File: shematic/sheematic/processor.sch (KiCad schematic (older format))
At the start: 15 parts, among them J1 Conn_01x05_Male, J2 Conn_01x05_Male, J3 Conn_01x05_Male, J4 Conn_01x07_Male, J5 Conn_01x02_Male, J6 Conn_01x07_Male, J7 Conn_01x07_Male, J8 Conn_01x07_Male, U1 E73-2G4M04S-52832

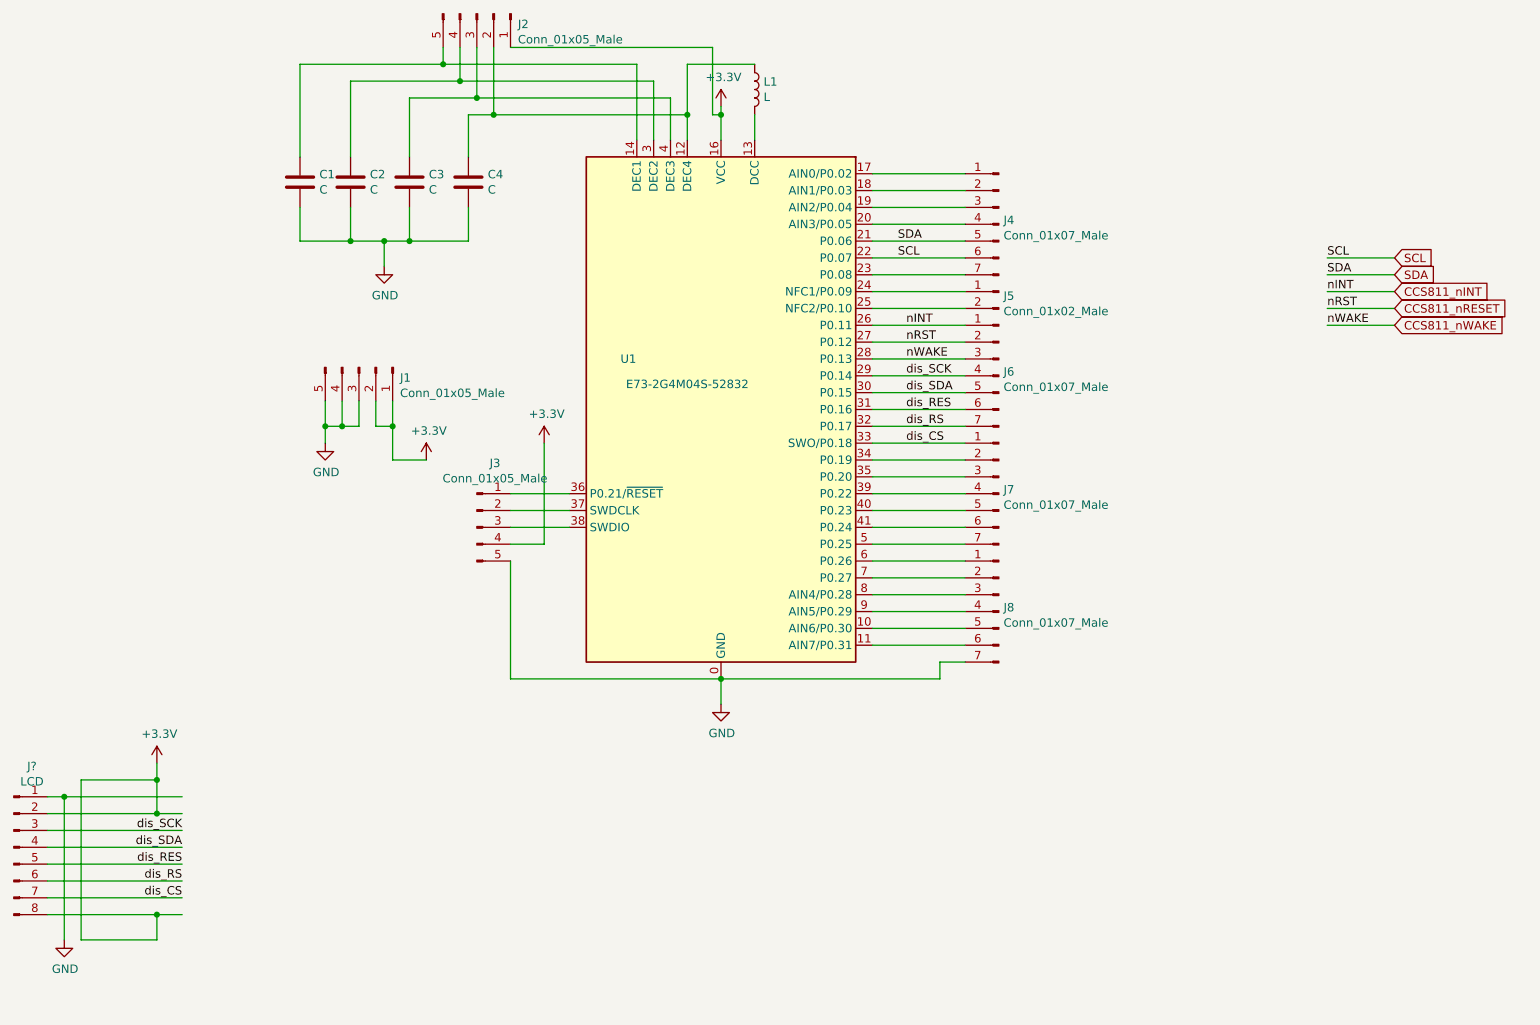
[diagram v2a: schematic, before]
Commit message: modify for warios drive
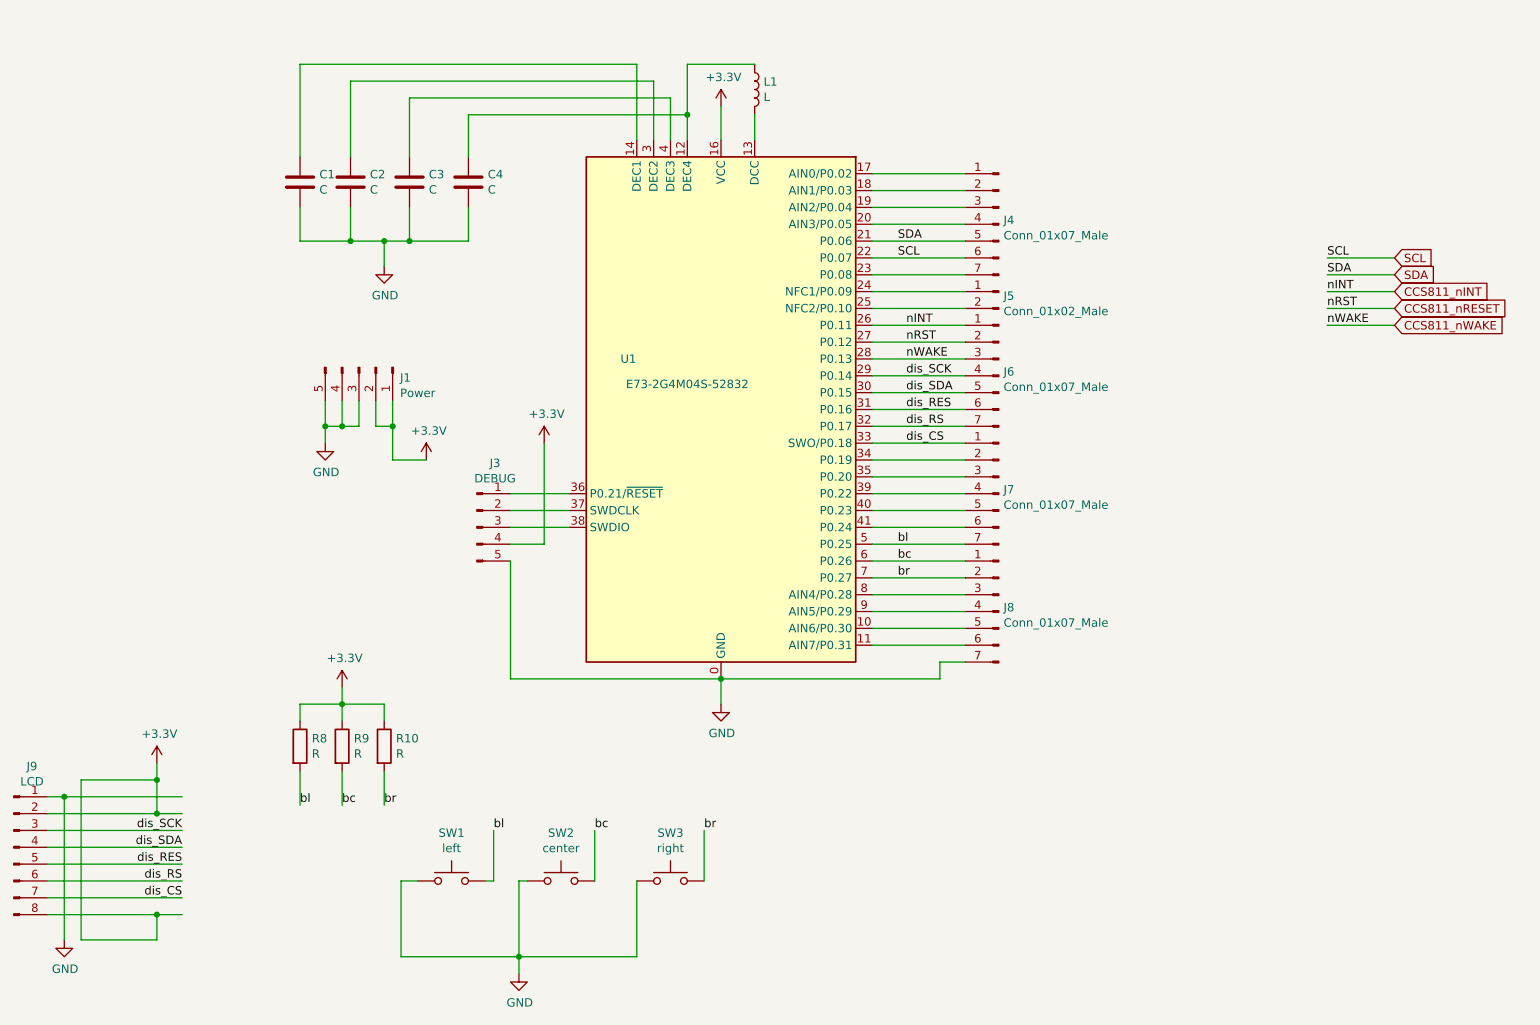
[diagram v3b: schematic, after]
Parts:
- removed J2: Conn_01x05_Male, symbol Connector:Conn_01x05_Male
- added R10, R8, R9: R, Resistor_SMD:R_0603_1608Metric_Pad1.05x0.95mm_HandSolder, symbol Device:R
- added SW1: left, Button_Switch_THT:SW_PUSH_6mm, symbol Switch:SW_Push
- added SW2: center, Button_Switch_THT:SW_PUSH_6mm, symbol Switch:SW_Push
- added SW3: right, Button_Switch_THT:SW_PUSH_6mm, symbol Switch:SW_Push
- C1, C2, C3, C4: footprint (none) -> Capacitor_SMD:C_0603_1608Metric_Pad1.08x0.95mm_HandSolder
- J1: value Conn_01x05_Male -> Power; footprint (none) -> Connector_PinHeader_2.54mm:PinHeader_1x05_P2.54mm_Vertical
- J3: value Conn_01x05_Male -> DEBUG; footprint (none) -> Connector_PinHeader_2.54mm:PinHeader_1x05_P2.54mm_Vertical
- J4, J6, J7, J8: footprint (none) -> Connector_PinHeader_2.54mm:PinHeader_1x07_P2.54mm_Vertical
- J5: footprint (none) -> Connector_PinHeader_2.54mm:PinHeader_1x02_P2.54mm_Vertical
- J9: renamed from J?; footprint (none) -> Connector_PinHeader_2.54mm:PinHeader_1x08_P2.54mm_Vertical
- L1: footprint (none) -> Inductor_SMD:L_0805_2012Metric_Pad1.15x1.40mm_HandSolder
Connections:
- net +3V3: now also R10.1, R8.1, R9.1
- net GND: now also SW1.1, SW2.1, SW3.1
- net bl: now reaches J7.7 (Pin_7), U1.5 (P0.25)
- net bl: now also R8.2, SW1.2
- net bc: now reaches J8.1 (Pin_1), U1.6 (P0.26)
- net bc: now also R9.2, SW2.2
- net br: now reaches J8.2 (Pin_2), U1.7 (P0.27)
- net br: now also R10.2, SW3.2
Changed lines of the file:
@@
 P 4700 3600
 F 0 "J3" H 4808 3981 50  0000 C CNN
-F 1 "Conn_01x05_Male" H 4808 3890 50  0000 C CNN
-F 2 "" H 4700 3600 50  0001 C CNN
+F 1 "DEBUG" H 4808 3890 50  0000 C CNN
+F 2 "Connector_PinHeader_2.54mm:PinHeader_1x05_P2.54mm_Vertical" H 4700 3600 50  0001 C CNN
 F 3 "~" H 4700 3600 50  0001 C CNN
 	1    4700 3600
@@
 	1    0    0    -1
 $EndComp
-Wire Wire Line
-	6150 1100 6150 1150
 $Comp
 L power:+3.3V #PWR04
@@
 F 0 "L1" H 6403 1046 50  0000 L CNN
 F 1 "L" H 6403 955 50  0000 L CNN
-F 2 "" H 6350 1000 50  0001 C CNN
+F 2 "Inductor_SMD:L_0805_2012Metric_Pad1.15x1.40mm_HandSolder" H 6350 1000 50  0001 C CNN
 F 3 "~" H 6350 1000 50  0001 C CNN
 	1    6350 1000
@@
 F 0 "C4" H 4765 1596 50  0000 L CNN
 F 1 "C" H 4765 1505 50  0000 L CNN
-F 2 "" H 4688 1400 50  0001 C CNN
+F 2 "Capacitor_SMD:C_0603_1608Metric_Pad1.08x0.95mm_HandSolder" H 4688 1400 50  0001 C CNN
 F 3 "~" H 4650 1550 50  0001 C CNN
 	1    4650 1550
@@
 F 0 "C3" H 4415 1596 50  0000 L CNN
 F 1 "C" H 4415 1505 50  0000 L CNN
-F 2 "" H 4338 1400 50  0001 C CNN
+F 2 "Capacitor_SMD:C_0603_1608Metric_Pad1.08x0.95mm_HandSolder" H 4338 1400 50  0001 C CNN
 F 3 "~" H 4300 1550 50  0001 C CNN
 	1    4300 1550
@@
 F 0 "C2" H 4065 1596 50  0000 L CNN
 F 1 "C" H 4065 1505 50  0000 L CNN
-F 2 "" H 3988 1400 50  0001 C CNN
+F 2 "Capacitor_SMD:C_0603_1608Metric_Pad1.08x0.95mm_HandSolder" H 3988 1400 50  0001 C CNN
 F 3 "~" H 3950 1550 50  0001 C CNN
 	1    3950 1550
@@
 F 0 "C1" H 3765 1596 50  0000 L CNN
 F 1 "C" H 3765 1505 50  0000 L CNN
-F 2 "" H 3688 1400 50  0001 C CNN
+F 2 "Capacitor_SMD:C_0603_1608Metric_Pad1.08x0.95mm_HandSolder" H 3688 1400 50  0001 C CNN
 F 3 "~" H 3650 1550 50  0001 C CNN
 	1    3650 1550
@@
 Wire Wire Line
 	4650 1400 4650 1150
-Wire Wire Line
-	4650 1150 4800 1150
 Connection ~ 5950 1150
 Wire Wire Line
@@
 	4300 1400 4300 1050
 Wire Wire Line
-	4300 1050 4700 1050
-Wire Wire Line
 	5850 1050 5850 1300
 Wire Wire Line
 	3950 1400 3950 950
 Wire Wire Line
-	3950 950  4600 950
-Wire Wire Line
 	5750 950  5750 1300
 Wire Wire Line
 	3650 1400 3650 850
-Wire Wire Line
-	3650 850  4500 850
 Wire Wire Line
 	5650 850  5650 1300
@@
 F 0 "J5" H 7772 2174 50  0000 R CNN
 F 1 "Conn_01x02_Male" H 7772 2083 50  0000 R CNN
-F 2 "" H 7800 2200 50  0001 C CNN
+F 2 "Connector_PinHeader_2.54mm:PinHeader_1x02_P2.54mm_Vertical" H 7800 2200 50  0001 C CNN
 F 3 "~" H 7800 2200 50  0001 C CNN
 	1    7800 2200
@@
 Wire Wire Line
 	7600 2300 7050 2300
-$Comp
-L Connector:Conn_01x05_Male J2
-U 1 1 602B2D83
-P 4700 550
-F 0 "J2" V 4762 794 50  0000 L CNN
-F 1 "Conn_01x05_Male" V 4853 794 50  0000 L CNN
-F 2 "" H 4700 550 50  0001 C CNN
-F 3 "~" H 4700 550 50  0001 C CNN
-	1    4700 550
-	0    1    1    0
-$EndComp
-Wire Wire Line
-	4500 750  4500 850
-Connection ~ 4500 850
-Wire Wire Line
-	4500 850  5650 850
-Wire Wire Line
-	4600 750  4600 950
-Connection ~ 4600 950
-Wire Wire Line
-	4600 950  5750 950
-Wire Wire Line
-	4700 750  4700 1050
-Connection ~ 4700 1050
-Wire Wire Line
-	4700 1050 5850 1050
-Wire Wire Line
-	4800 750  4800 1150
-Connection ~ 4800 1150
-Wire Wire Line
-	4800 1150 5950 1150
-Wire Wire Line
-	4900 750  6100 750
-Wire Wire Line
-	6100 750  6100 1150
-Wire Wire Line
-	6100 1150 6150 1150
-Connection ~ 6150 1150
-Wire Wire Line
-	6150 1150 6150 1300
 $Comp
 L Connector:Conn_01x07_Male J4
@@
 F 0 "J4" H 7772 1824 50  0000 R CNN
 F 1 "Conn_01x07_Male" H 7772 1733 50  0000 R CNN
-F 2 "" H 7800 1800 50  0001 C CNN
+F 2 "Connector_PinHeader_2.54mm:PinHeader_1x07_P2.54mm_Vertical" H 7800 1800 50  0001 C CNN
 F 3 "~" H 7800 1800 50  0001 C CNN
 	1    7800 1800
@@
 F 0 "J6" H 7772 2724 50  0000 R CNN
 F 1 "Conn_01x07_Male" H 7772 2633 50  0000 R CNN
-F 2 "" H 7800 2700 50  0001 C CNN
+F 2 "Connector_PinHeader_2.54mm:PinHeader_1x07_P2.54mm_Vertical" H 7800 2700 50  0001 C CNN
 F 3 "~" H 7800 2700 50  0001 C CNN
 	1    7800 2700
@@
 F 0 "J7" H 7772 3424 50  0000 R CNN
 F 1 "Conn_01x07_Male" H 7772 3333 50  0000 R CNN
-F 2 "" H 7800 3400 50  0001 C CNN
+F 2 "Connector_PinHeader_2.54mm:PinHeader_1x07_P2.54mm_Vertical" H 7800 3400 50  0001 C CNN
 F 3 "~" H 7800 3400 50  0001 C CNN
 	1    7800 3400
@@
 F 0 "J8" H 7772 4124 50  0000 R CNN
 F 1 "Conn_01x07_Male" H 7772 4033 50  0000 R CNN
-F 2 "" H 7800 4100 50  0001 C CNN
+F 2 "Connector_PinHeader_2.54mm:PinHeader_1x07_P2.54mm_Vertical" H 7800 4100 50  0001 C CNN
 F 3 "~" H 7800 4100 50  0001 C CNN
 	1    7800 4100
@@
 P 4000 2650
 F 0 "J1" V 4062 2894 50  0000 L CNN
-F 1 "Conn_01x05_Male" V 4153 2894 50  0000 L CNN
-F 2 "" H 4000 2650 50  0001 C CNN
+F 1 "Power" V 4153 2894 50  0000 L CNN
+F 2 "Connector_PinHeader_2.54mm:PinHeader_1x05_P2.54mm_Vertical" H 4000 2650 50  0001 C CNN
 F 3 "~" H 4000 2650 50  0001 C CNN
 	1    4000 2650
@@
 nWAKE
 $Comp
-L Connector:Conn_01x08_Male J?
+L Connector:Conn_01x08_Male J9
 U 1 1 60323D13
 P 1950 5500
-F 0 "J?" H 2058 5981 50  0000 C CNN
+F 0 "J9" H 2058 5981 50  0000 C CNN
 F 1 "LCD" H 2058 5890 50  0000 C CNN
-F 2 "" H 1950 5500 50  0001 C CNN
+F 2 "Connector_PinHeader_2.54mm:PinHeader_1x08_P2.54mm_Vertical" H 1950 5500 50  0001 C CNN
 F 3 "~" H 1950 5500 50  0001 C CNN
 	1    1950 5500
@@
 	2150 5800 2950 5800
 $Comp
-L power:+3.3V #PWR?
+L power:+3.3V #PWR0111
 U 1 1 6033BA4B
 P 2800 5000
-F 0 "#PWR?" H 2800 4850 50  0001 C CNN
+F 0 "#PWR0111" H 2800 4850 50  0001 C CNN
 F 1 "+3.3V" H 2815 5173 50  0000 C CNN
 F 2 "" H 2800 5000 50  0001 C CNN
@@
 	2800 5300 2950 5300
 $Comp
-L power:GND #PWR?
+L power:GND #PWR0112
 U 1 1 6034B03A
 P 2250 6050
-F 0 "#PWR?" H 2250 5800 50  0001 C CNN
+F 0 "#PWR0112" H 2250 5800 50  0001 C CNN
 F 1 "GND" H 2255 5877 50  0000 C CNN
 F 2 "" H 2250 6050 50  0001 C CNN
@@
 Text Label 7250 3100 0    50   ~ 0
 dis_CS
+Wire Wire Line
+	4350 5700 4250 5700
+Wire Wire Line
+	5000 5700 4950 5700
+Wire Wire Line
+	4950 6150 4250 6150
+Wire Wire Line
+	5650 6150 4950 6150
+Connection ~ 4950 6150
+$Comp
+L power:GND #PWR0113
+U 1 1 602D8CC3
+P 4950 6250
+F 0 "#PWR0113" H 4950 6000 50  0001 C CNN
+F 1 "GND" H 4955 6077 50  0000 C CNN
+F 2 "" H 4950 6250 50  0001 C CNN
+F 3 "" H 4950 6250 50  0001 C CNN
+	1    4950 6250
+	1    0    0    -1
+$EndComp
+Wire Wire Line
+	4950 6250 4950 6150
+$Comp
+L Device:R R8
+U 1 1 602DDDED
+P 3650 4900
+F 0 "R8" H 3720 4946 50  0000 L CNN
+F 1 "R" H 3720 4855 50  0000 L CNN
+F 2 "Resistor_SMD:R_0603_1608Metric_Pad1.05x0.95mm_HandSolder" V 3580 4900 50  0001 C CNN
+F 3 "~" H 3650 4900 50  0001 C CNN
+	1    3650 4900
+	1    0    0    -1
+$EndComp
+$Comp
+L Device:R R9
+U 1 1 602DE809
+P 3900 4900
+F 0 "R9" H 3970 4946 50  0000 L CNN
+F 1 "R" H 3970 4855 50  0000 L CNN
+F 2 "Resistor_SMD:R_0603_1608Metric_Pad1.05x0.95mm_HandSolder" V 3830 4900 50  0001 C CNN
+F 3 "~" H 3900 4900 50  0001 C CNN
+	1    3900 4900
+	1    0    0    -1
+$EndComp
+$Comp
+L Device:R R10
+U 1 1 602DE988
+P 4150 4900
+F 0 "R10" H 4220 4946 50  0000 L CNN
+F 1 "R" H 4220 4855 50  0000 L CNN
+F 2 "Resistor_SMD:R_0603_1608Metric_Pad1.05x0.95mm_HandSolder" V 4080 4900 50  0001 C CNN
+F 3 "~" H 4150 4900 50  0001 C CNN
+	1    4150 4900
+	1    0    0    -1
+$EndComp
+$Comp
+L power:+3.3V #PWR0114
+U 1 1 602DEB60
+P 3900 4550
+F 0 "#PWR0114" H 3900 4400 50  0001 C CNN
+F 1 "+3.3V" H 3915 4723 50  0000 C CNN
+F 2 "" H 3900 4550 50  0001 C CNN
+F 3 "" H 3900 4550 50  0001 C CNN
+	1    3900 4550
+	1    0    0    -1
+$EndComp
+Wire Wire Line
+	3650 4750 3650 4650
+Wire Wire Line
+	3650 4650 3900 4650
+Wire Wire Line
+	3900 4650 3900 4550
+Wire Wire Line
+	4150 4750 4150 4650
+Wire Wire Line
+	4150 4650 3900 4650
+Connection ~ 3900 4650
+Wire Wire Line
+	3900 4750 3900 4650
+Wire Wire Line
+	3650 5050 3650 5250
+Wire Wire Line
+	3900 5050 3900 5250
+Wire Wire Line
+	4150 5050 4150 5250
+Text Label 3650 5250 0    50   ~ 0
+bl
+Text Label 3900 5250 0    50   ~ 0
+bc
+Text Label 4150 5250 0    50   ~ 0
+br
+Wire Wire Line
+	4800 5700 4750 5700
+Wire Wire Line
+	4800 5400 4800 5700
+Text Label 4800 5400 0    50   ~ 0
+bl
+Text Label 5400 5400 0    50   ~ 0
+bc
+Text Label 6050 5400 0    50   ~ 0
+br
+Wire Wire Line
+	5400 5400 5400 5700
+Wire Wire Line
+	5650 5700 5650 6150
+Wire Wire Line
+	6050 5400 6050 5700
+Wire Wire Line
+	4250 5700 4250 6150
+Wire Wire Line
+	4950 5700 4950 6150
+$Comp
+L Switch:SW_Push SW1
+U 1 1 603416AF
+P 4550 5700
+F 0 "SW1" H 4550 5985 50  0000 C CNN
+F 1 "left" H 4550 5894 50  0000 C CNN
+F 2 "Button_Switch_THT:SW_PUSH_6mm" H 4550 5900 50  0001 C CNN
+F 3 "~" H 4550 5900 50  0001 C CNN
+	1    4550 5700
+	1    0    0    -1
+$EndComp
+$Comp
+L Switch:SW_Push SW2
+U 1 1 6034262E
+P 5200 5700
+F 0 "SW2" H 5200 5985 50  0000 C CNN
+F 1 "center" H 5200 5894 50  0000 C CNN
+F 2 "Button_Switch_THT:SW_PUSH_6mm" H 5200 5900 50  0001 C CNN
+F 3 "~" H 5200 5900 50  0001 C CNN
+	1    5200 5700
+	1    0    0    -1
+$EndComp
+$Comp
+L Switch:SW_Push SW3
+U 1 1 60342C9A
+P 5850 5700
+F 0 "SW3" H 5850 5985 50  0000 C CNN
+F 1 "right" H 5850 5894 50  0000 C CNN
+F 2 "Button_Switch_THT:SW_PUSH_6mm" H 5850 5900 50  0001 C CNN
+F 3 "~" H 5850 5900 50  0001 C CNN
+	1    5850 5700
+	1    0    0    -1
+$EndComp
+Text Label 7200 3700 0    50   ~ 0
+bl
+Text Label 7200 3800 0    50   ~ 0
+bc
+Text Label 7200 3900 0    50   ~ 0
+br
+Wire Wire Line
+	4650 1150 5950 1150
+Wire Wire Line
+	6150 1100 6150 1300
+Wire Wire Line
+	4300 1050 5850 1050
+Wire Wire Line
+	3950 950  5750 950
+Wire Wire Line
+	3650 850  5650 850
 $EndSCHEMATC
